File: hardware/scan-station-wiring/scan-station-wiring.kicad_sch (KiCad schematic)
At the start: 27 parts, among them J1 CYD SPI, J2 NFC Antenna Board, J4 NFC Antenna B, J5 USB-C Power, J6 Load Cell, Q1 TVDD_SW_A, Q2 TVDD_SW_B, U1 ESP32-S3-DevKitC-1, U2 ADS1220IPWR, U3 AHT20, U4 PN5180A0HN, U5 AS7341-DLGM, U6 AMS1117-3.3

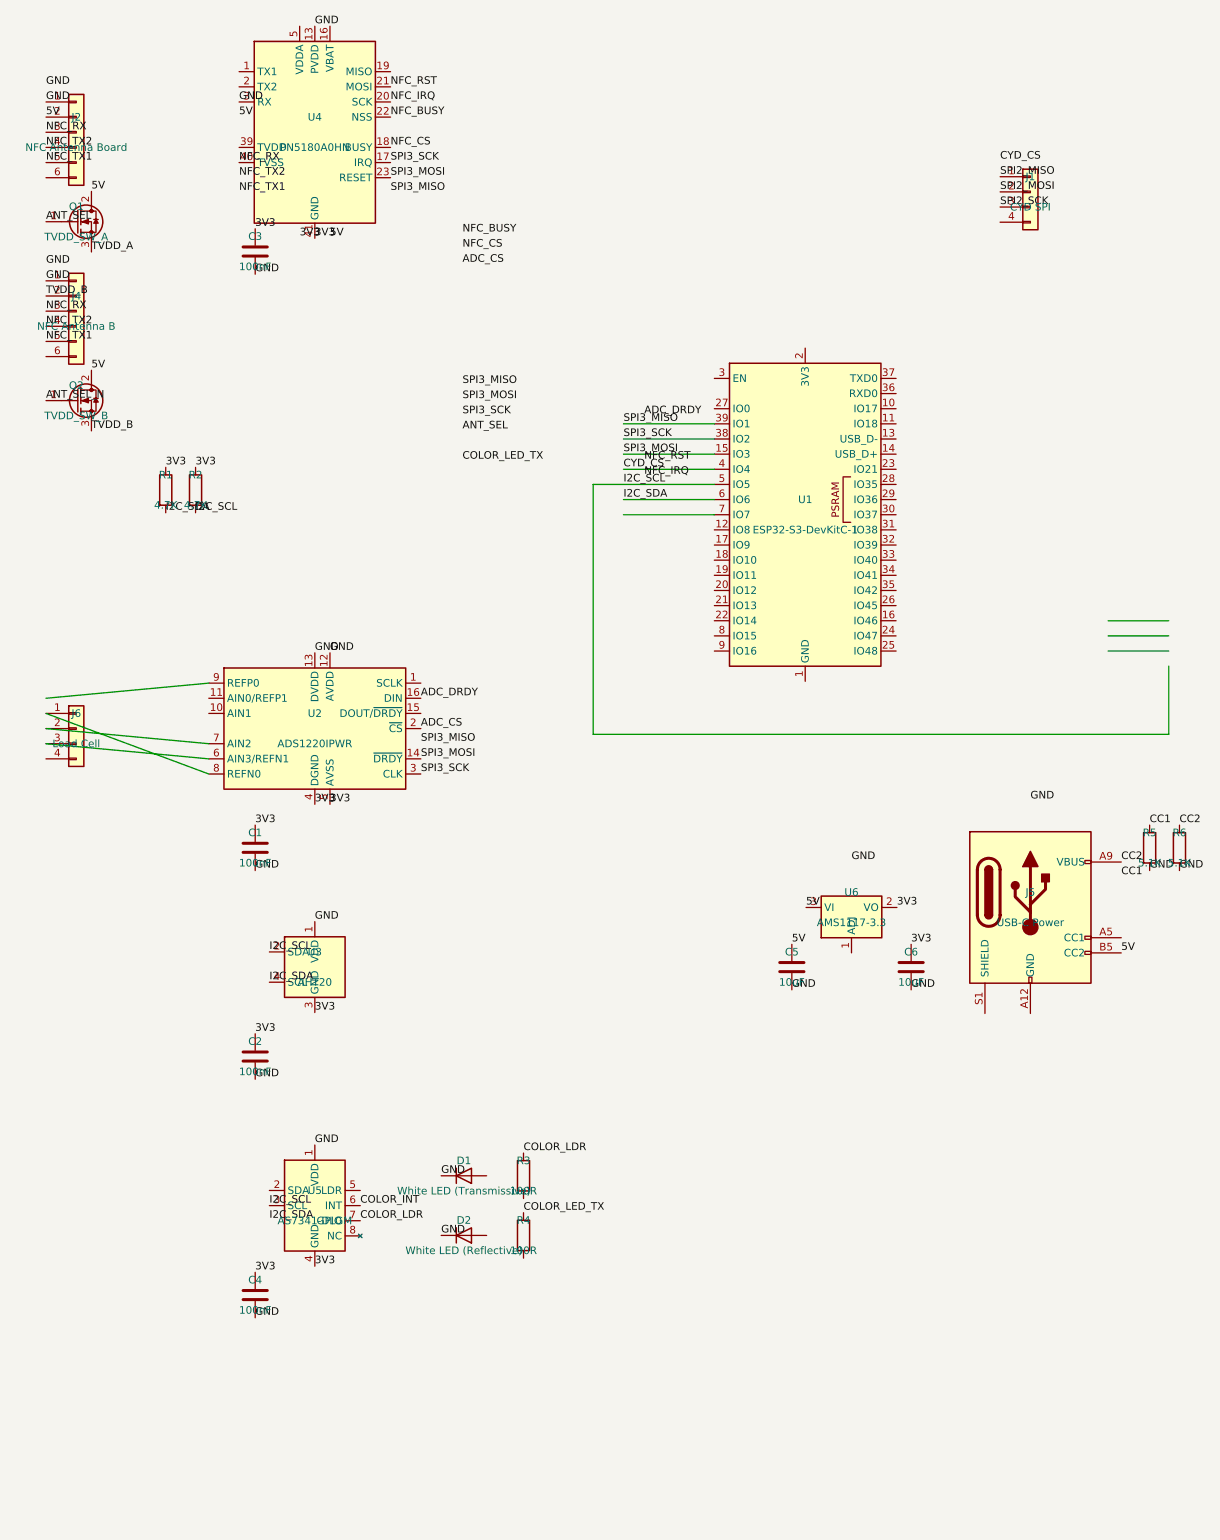
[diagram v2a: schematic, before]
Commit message: feat: add RGB LED support to antenna boards and external header
- Upgrade antenna connectors from 6-pin to 7-pin (add LED_DATA)
- Add J3 external RGB LED header (5V, LED_DATA, GND)
- Single LED_DATA GPIO (IO38) drives all pixels in parallel
- Works with 0, 1, or 2 antenna boards plus external header
- WS2812B/SK6812 addressable RGB pixels

Co-Authored-By: Claude Opus 4.6 (1M context) <noreply@anthropic.com>
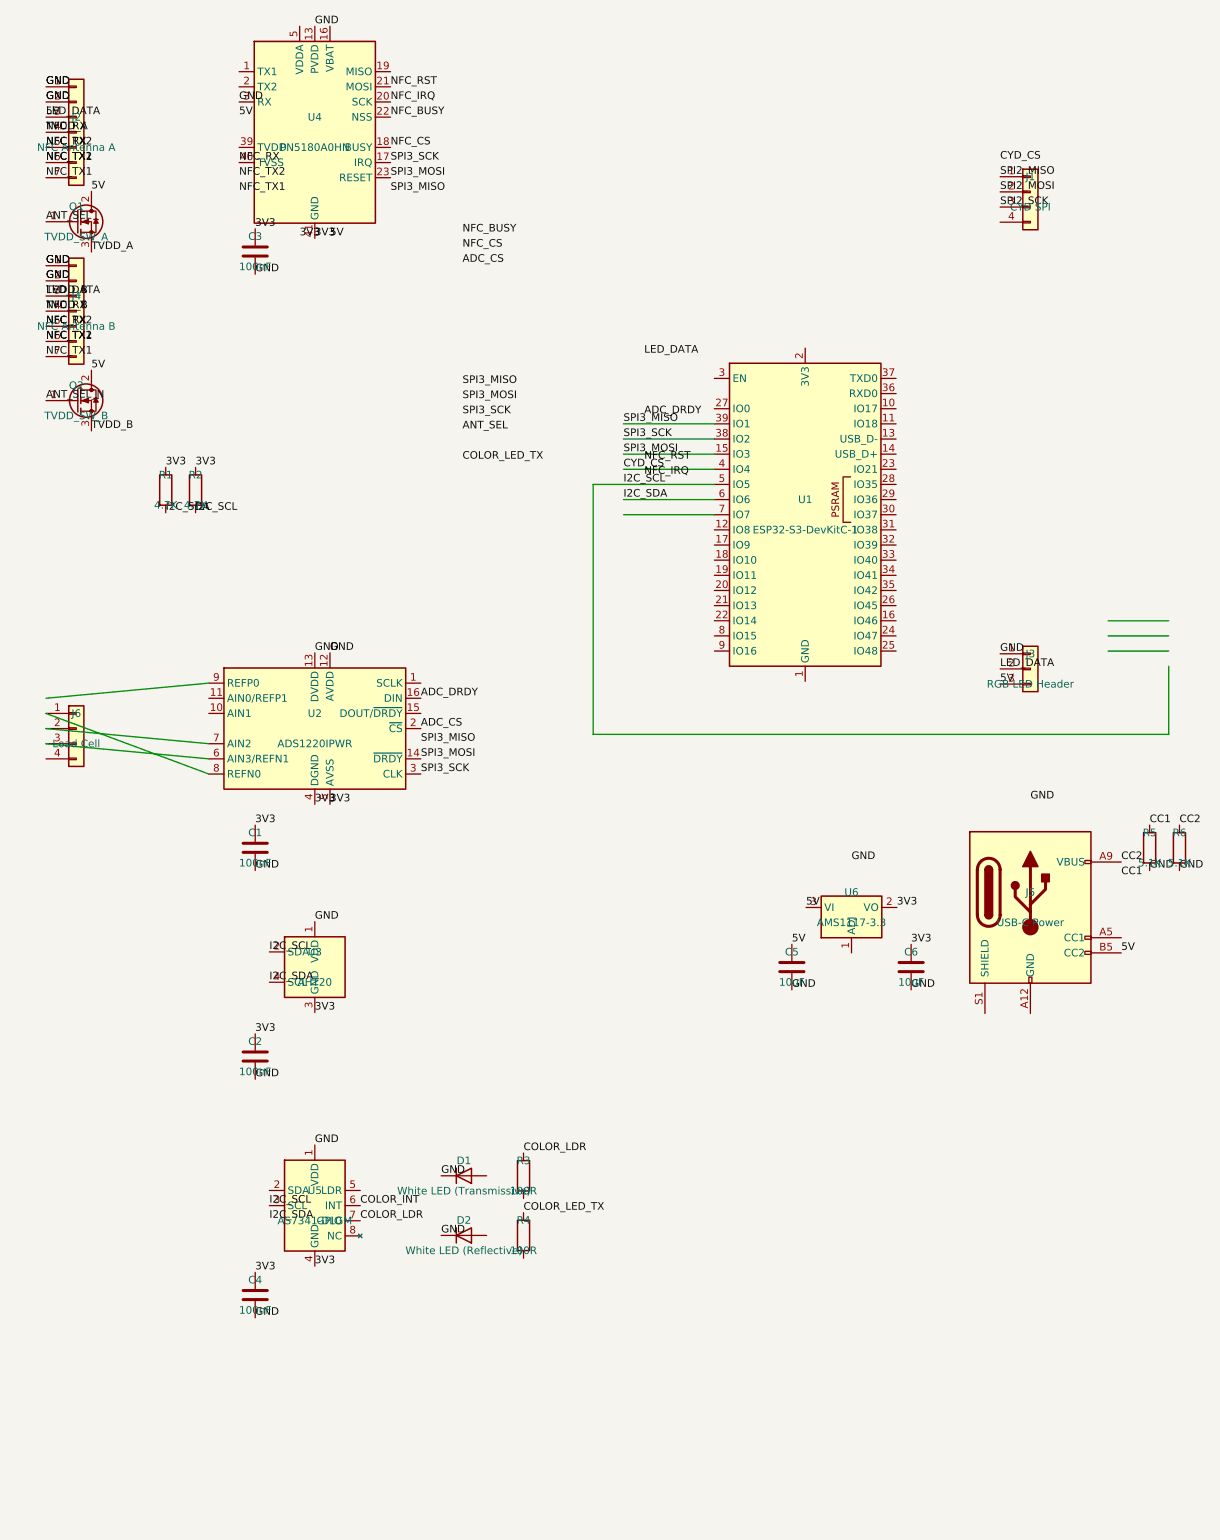
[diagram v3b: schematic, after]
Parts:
- removed J2: NFC Antenna Board, symbol Connector_Generic:Conn_01x06
- removed J4: NFC Antenna B, symbol Connector_Generic:Conn_01x06
- added J2: NFC Antenna A, symbol Connector_Generic:Conn_01x07
- added J3: RGB LED Header, symbol Connector_Generic:Conn_01x03
- added J4: NFC Antenna B, symbol Connector_Generic:Conn_01x07
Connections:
- net NFC_RX is gone; now on net 5V: U4.40 (TVSS)
- net TVDD_A is gone; now on net 5V: Q1.3 (S)
- net TVDD_B is gone; now on net 5V: Q2.3 (S)
- net 5V: now also J2.3 (Pin_3), J2.4 (Pin_4), J2.5 (Pin_5), J2.6 (Pin_6), J2.7 (Pin_7), J3.2 (Pin_2), J3.3 (Pin_3), J4.3 (Pin_3), J4.4 (Pin_4), J4.5 (Pin_5), J4.6 (Pin_6), J4.7 (Pin_7)
- net GND: now also J2.1 (Pin_1), J2.2 (Pin_2), J3.1 (Pin_1), J4.1 (Pin_1), J4.2 (Pin_2)

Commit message: feat: add CAN bus, I2C1 expansion, TOF connector, RGB LED header
- SN65HVD230DR CAN transceiver (C12084, $0.80, Preferred/free assembly)
  ESP32 TWAI controller on IO41/IO42, CAN bus connector (CANH/CANL/5V/GND)
- Second I2C bus (I2C1) on IO39/IO40 with 4.7K pull-ups
  Dedicated to TOF sensor and expansion header (Qwiic-compatible)
- J8: I2C1 expansion header (3V3/GND/SDA/SCL)
- J9: TOF sensor connector (3V3/GND/SDA/SCL) on I2C1
- J3: External RGB LED header (5V/LED_DATA/GND)
  Single LED_DATA net shared with both antenna board connectors
  Works with 0, 1, or 2 antenna boards connected

Co-Authored-By: Claude Opus 4.6 (1M context) <noreply@anthropic.com>
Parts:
- added C7: 100nF, symbol Device:C
- added J7: CAN Bus, symbol Connector_Generic:Conn_01x04
- added J8: I2C1 Expansion, symbol Connector_Generic:Conn_01x04
- added J9: TOF Sensor (I2C1), symbol Connector_Generic:Conn_01x04
- added R7, R8: 4.7K, symbol Device:R
- added U7: SN65HVD230DR, symbol Interface_CAN_LIN:SN65HVD230
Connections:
- net 3V3: now also C7.1, J8.3 (Pin_3), J9.3 (Pin_3), R7.1, R8.1
- net 5V: now also J7.1 (Pin_1)
- net GND: now also C7.2, J8.2 (Pin_2), J9.2 (Pin_2)
- new net CANH: J7.3 (Pin_3), U7.7 (CANH)
- new net CANL: J7.2 (Pin_2)
- new net CAN_RX: U7.4 (R)
- new net CAN_TX: U7.5 (Vref)
- new net I2C1_SCL: R8.2
- new net I2C1_SDA: J8.1 (Pin_1), J9.1 (Pin_1), R7.2

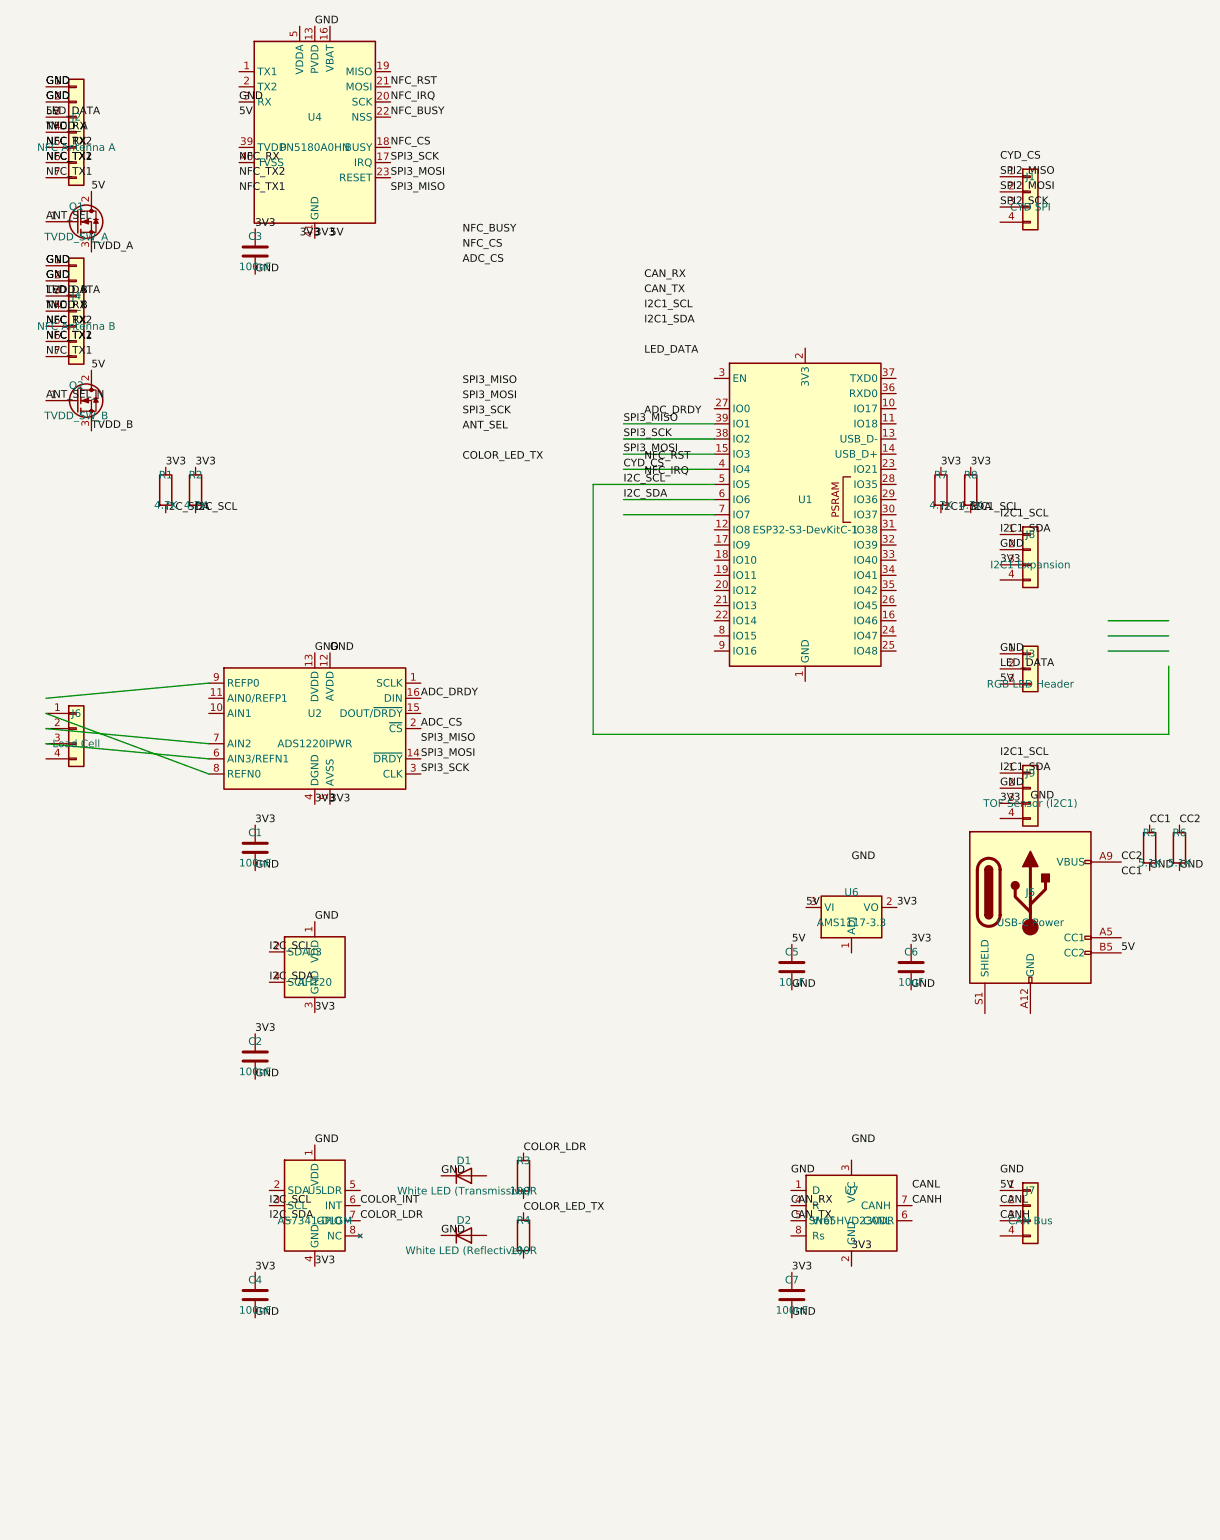
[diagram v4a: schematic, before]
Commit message: feat: add datasheet-required passives, level shifting, CYD power
Based on Adafruit AS7341 reference design and sensor datasheets:

AS7341 corrections:
- AMS1117-1.8 LDO (AS7341 runs at 1.8V, not 3.3V)
- BSS138 I2C level shifters (Q3/Q4) with 10K pull-ups both sides
- 100nF + 10uF decoupling on 1.8V rail
- INT pull-up to 3.3V

ADS1220 additions:
- 1uF caps on AVDD and DVDD (per TI datasheet)
- 100nF across REFP0-REFN0 reference pins

PN5180 additions:
- 27.12MHz crystal (Y1) — external oscillator required
- 80uF + 100nF on VBAT
- 10uF on TVDD

CYD display connection:
- Split into J1A (expansion SPI) + J1B (UART power+handshake)
- 5V power to CYD via UART connector
- CYD_READY handshake GPIO (IO43→IO2)
- 10K pull-ups on SPI2 MOSI/MISO/CS lines

Co-Authored-By: Claude Opus 4.6 (1M context) <noreply@anthropic.com>
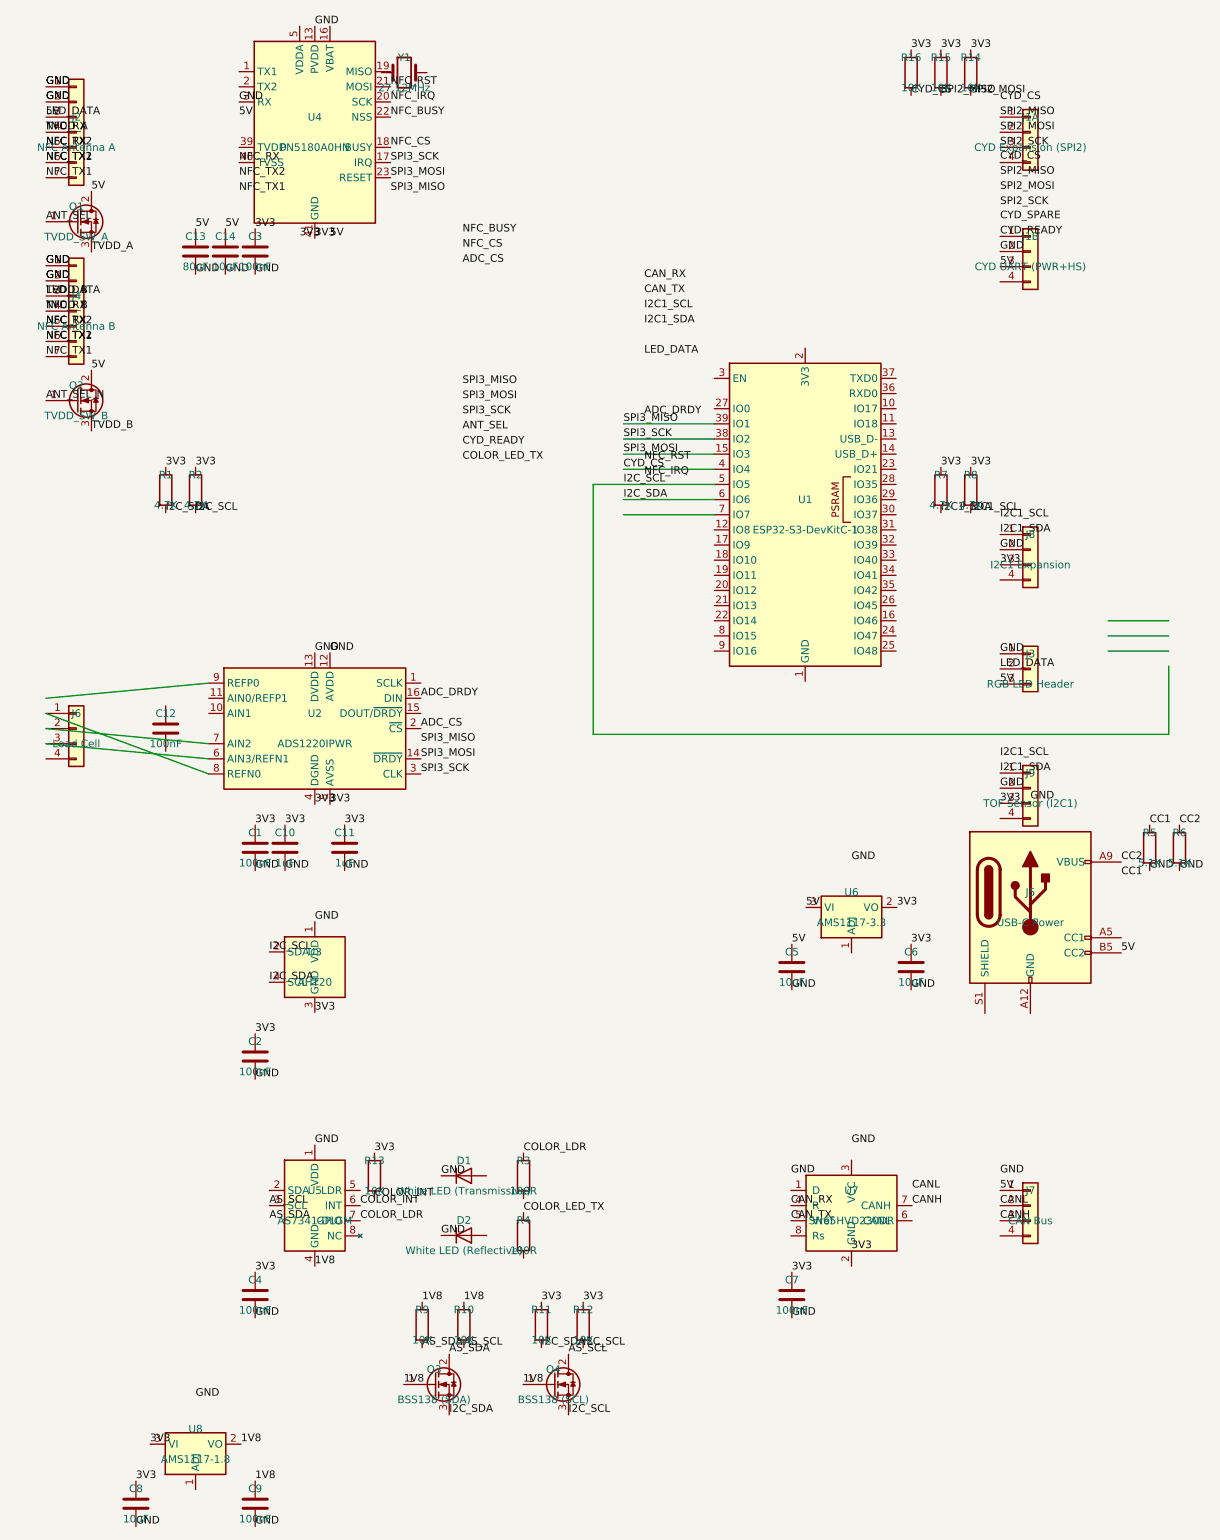
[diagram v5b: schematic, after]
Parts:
- removed J1: CYD SPI, symbol Connector_Generic:Conn_01x04
- added C10, C11: 1uF, symbol Device:C
- added C12, C9: 100nF, symbol Device:C
- added C13: 80uF, symbol Device:C
- added C14, C8: 10uF, symbol Device:C
- added J1A: CYD Expansion (SPI2), symbol Connector_Generic:Conn_01x04
- added J1B: CYD UART (PWR+HS), symbol Connector_Generic:Conn_01x04
- added Q3: BSS138 (SDA), symbol Transistor_FET:Q_NMOS_GDS
- added Q4: BSS138 (SCL), symbol Transistor_FET:Q_NMOS_GDS
- added R10, R11, R12, R13, R14, R15, R16, R9: 10K, symbol Device:R
- added U8: AMS1117-1.8, symbol Regulator_Linear:AMS1117
- added Y1: 27.12MHz, symbol Device:Crystal
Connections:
- net 3V3: now also C10.1, C11.1, C8.1, R11.1, R12.1, R13.1, R14.1, R15.1, R16.1, U8.3 (VI); no longer U5.4 (GND)
- net 5V: now also C13.1, C14.1, J1B.3 (Pin_3)
- net COLOR_INT: now also R13.2
- net CYD_CS: now also R16.2
- net GND: now also C10.2, C11.2, C13.2, C14.2, C8.2, C9.2, J1B.2 (Pin_2)
- net I2C_SCL: now also Q4.3 (S), R12.2; no longer U5.3 (SCL)
- net I2C_SDA: now also Q3.3 (S), R11.2
- net SPI2_MISO: now also J1A.1 (Pin_1), R15.2
- net SPI2_MOSI: now also J1A.2 (Pin_2), R14.2
- net SPI2_SCK: now also J1A.3 (Pin_3)
- new net 1V8: C9.1, Q3.1 (G), Q4.1 (G), R10.1, R9.1, U5.4 (GND), U8.2 (VO)
- new net AS_SCL: Q4.2 (D), R10.2, U5.3 (SCL)
- new net AS_SDA: Q3.2 (D), R9.2
- new net CYD_READY: J1B.1 (Pin_1)
